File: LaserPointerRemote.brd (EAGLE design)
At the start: 24.5 x 45.5 mm, 34 parts, among them IC1 MEGA8-AI, IC2 MCP1640, J1 AVR_SPI_PRG_6NS, U1 2N7002, X1 22-05-7028-02, X3 22-23-2031

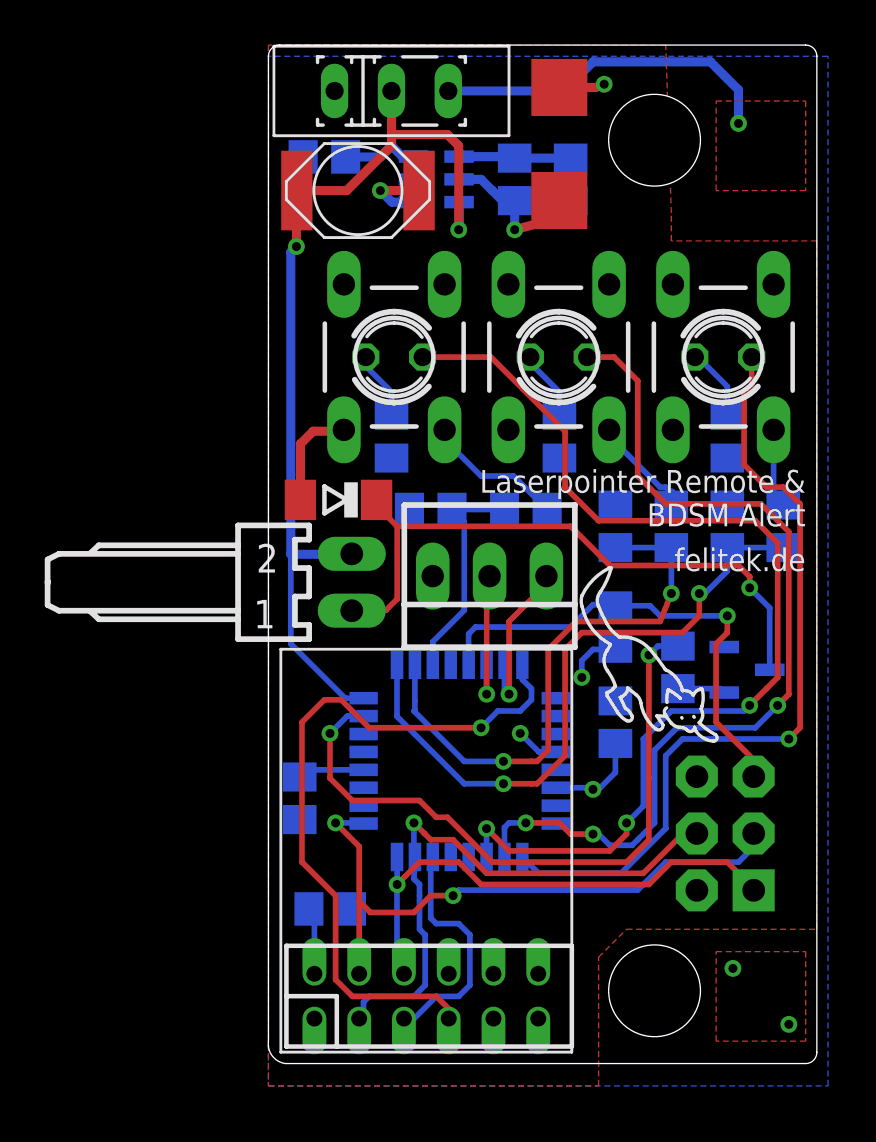
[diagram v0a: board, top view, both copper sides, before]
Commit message: Refactored PCB to fit the strapupox
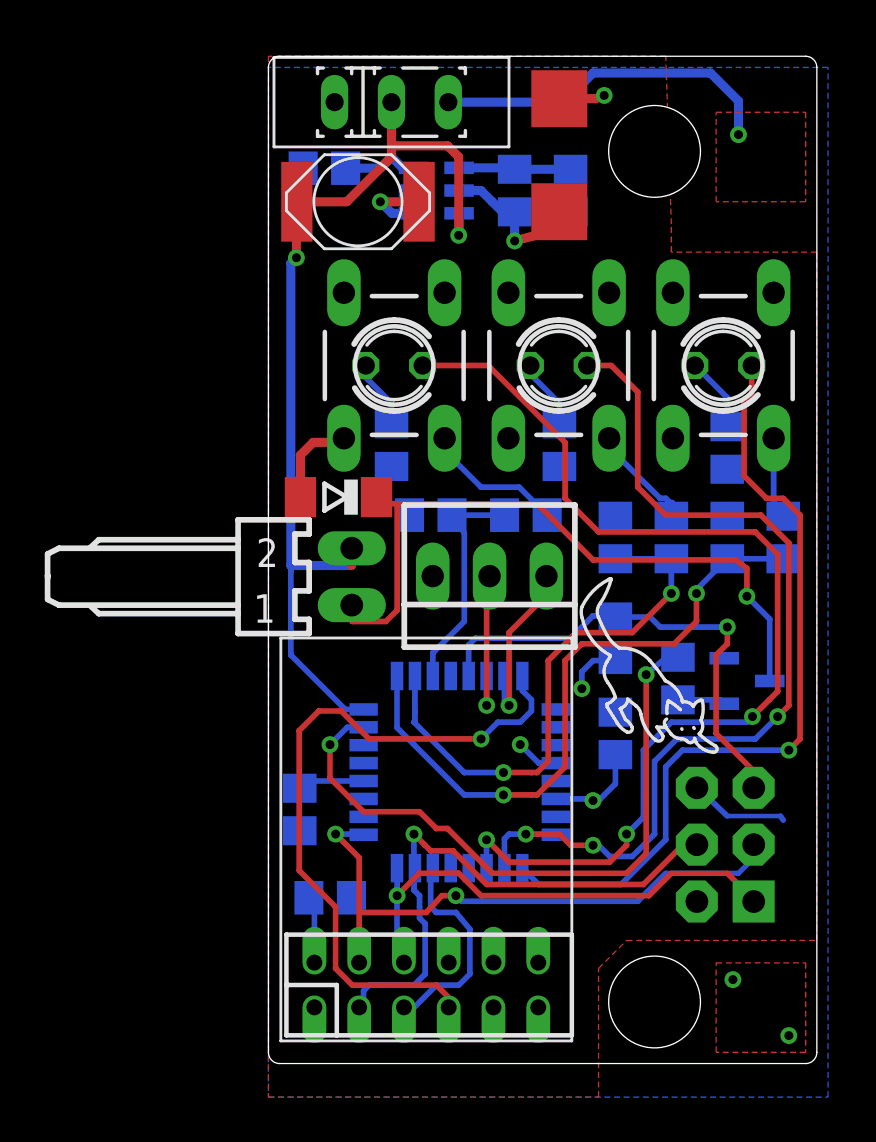
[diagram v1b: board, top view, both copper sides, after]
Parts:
- moved C1 0.50 mm to (15.5, 14.8)
- moved C2 0.50 mm to (1.40, 11.3)
- moved C3 0.50 mm to (2.76, 7.41)
- moved C4 0.50 mm to (2.50, 40.0)
- moved C5 0.50 mm to (13.0, 40.6)
- moved C6 0.50 mm to (20.5, 23.5)
- moved C7 0.50 mm to (15.5, 23.5)
- moved IC1 0.50 mm to (8.54, 13.0)
- moved IC2 0.50 mm to (7.50, 39.0)
- moved J1 0.50 mm to (20.4, 9.78)
- moved L2 0.50 mm to (4.00, 38.5)
- moved R1 0.50 mm to (15.5, 19.0)
- moved R10 0.50 mm to (18.0, 23.5)
- moved R12 0.50 mm to (23.0, 23.5)
- moved R2 0.50 mm to (18.3, 17.2)
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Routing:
- net GND: track 6.73 -> 10.7 mm
- net N$2: track 28.3 -> 31.1 mm
- net SCK: track 28.1 -> 26.9 mm
- net SEL: track 10.6 -> 9.54 mm
- net MOSI: track 25.7 -> 24.7 mm
- net MISO: track 23.7 -> 22.7 mm
- net VIN: track 49.0 -> 50.0 mm
- net INT0: track 31.6 -> 30.8 mm
- net INPUT2: track 25.1 -> 24.5 mm
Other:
- board size 24.5 x 45.5 mm -> 24.5 x 45 mm
- board text removed: "BDSM Alert"
- board text removed: "Laserpointer Remote &"

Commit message: Changed VCC to 5V instead of 3.3V Added NPN transistor instead of mosfet Connected AVCC
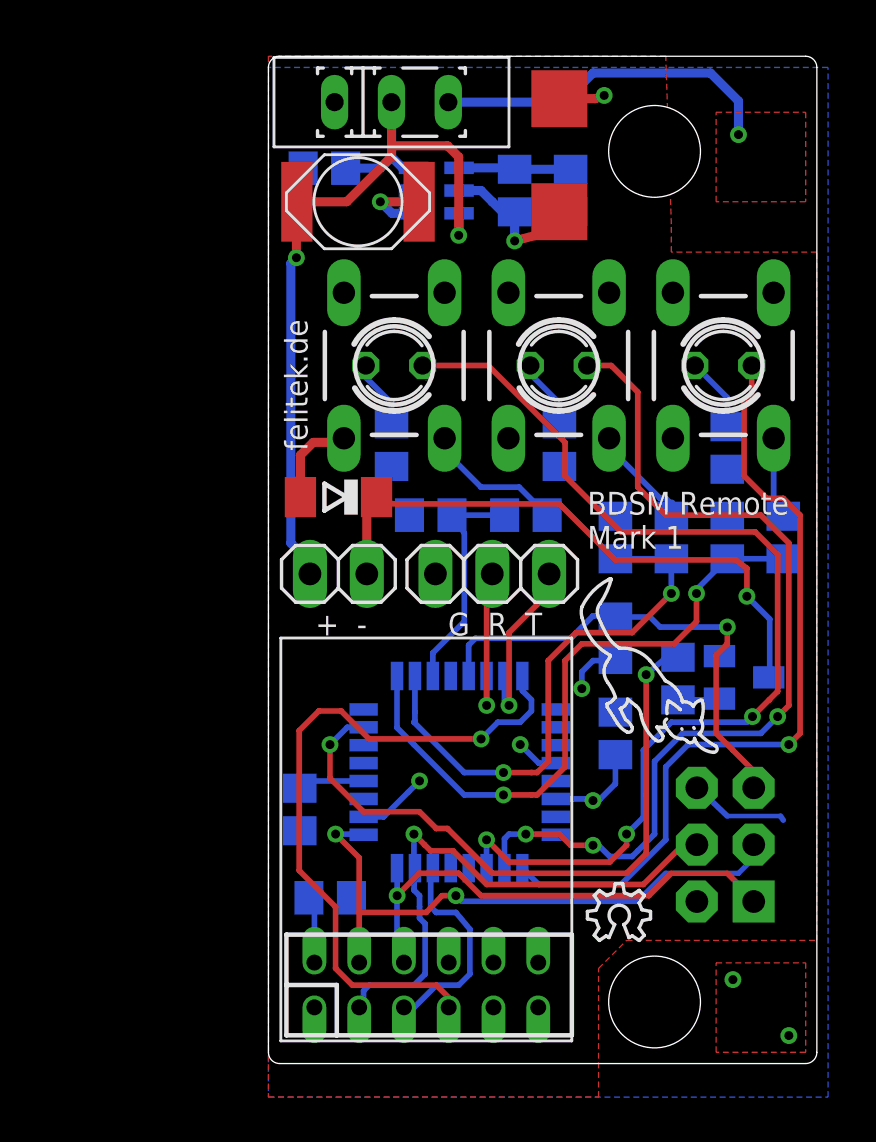
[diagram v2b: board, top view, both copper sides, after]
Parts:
- removed U1: 2N7002, SteveMarple:SOT23-3-ROTATED
- removed X1: 22-05-7028-02, con-molex:7395-02
- removed X3: 22-23-2031, con-molex:22-23-2031
- added JP1: (no value), pinhead:1X02
- added JP2: (no value), pinhead:1X03
- added T1: BC818, transistor:SOT23-BEC
- added U$2: (no value), ohw-logo:OSHW_6X100_NOTEXT
- R6: value 97.6k -> 100k
- R7: value 56.2k -> 33k
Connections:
- removed net AVCC: IC1.18
- net GND: now also JP2.3, T1.E; no longer U1.2, X3.3
- net N$1: now also T1.B; no longer U1.1
- net N$2: now also JP1.1, T1.C; no longer U1.3, X1.1
- net RXD: now also JP2.2; no longer X3.2
- net TXD: now also JP2.1; no longer X3.1
- net VCC: now also IC1.18
- net VIN: now also JP1.2; no longer IC1.24, X1.2
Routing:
- net VIN: track 50.0 -> 38.2 mm
- net N$2: track 31.1 -> 27.3 mm
- net VCC: track 18.4 -> 21.6 mm, vias 4 -> 5
- net LED3: track 46.9 -> 46.3 mm
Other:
- board text added: "+ -"
- board text added: "BDSM Remote Mark 1"
- board text added: "G R T"

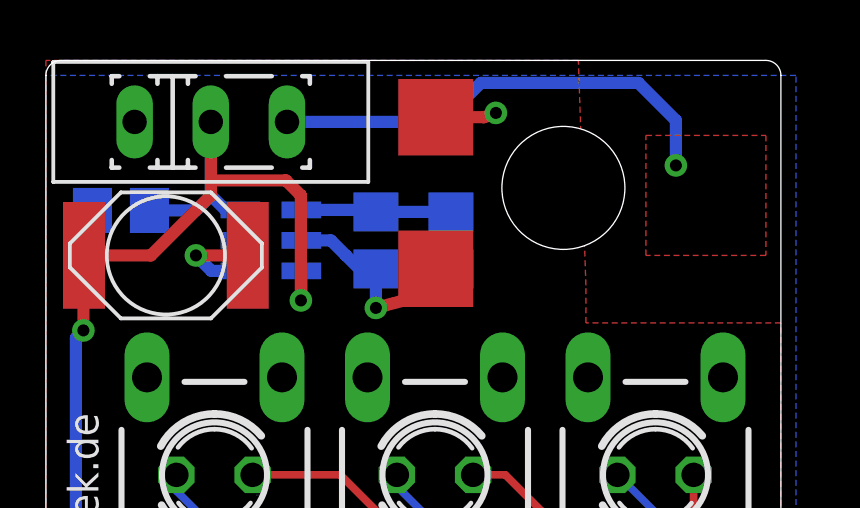
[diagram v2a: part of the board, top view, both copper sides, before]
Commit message: Use X7R output cap instead of a tantalum one
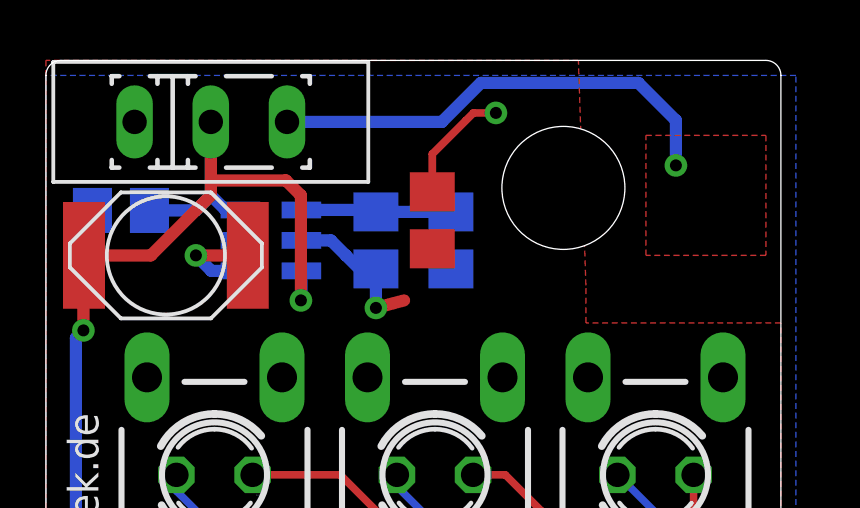
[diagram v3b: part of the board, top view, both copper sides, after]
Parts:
- C5: device rcl:C/6032-28R -> rcl:C0805
- moved C5 0.92 mm to (12.9, 39.7), turned to 90 degrees
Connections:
- net GND: now also C5.2; no longer C5.-
- net VCC: now also C5.1; no longer C5.+
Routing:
- net GND: track 10.7 -> 12.6 mm
- net VCC: track 21.6 -> 20.1 mm
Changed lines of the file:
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@@
 <grid distance="1" unitdist="mm" unit="mm" style="lines" multiple="1" display="no" altdistance="0.125" altunitdist="mm" altunit="mm"/>
 <layers>
-<layer number="1" name="Top" color="4" fill="1" visible="no" active="yes"/>
+<layer number="1" name="Top" color="4" fill="1" visible="yes" active="yes"/>
 <layer number="2" name="Route2" color="1" fill="3" visible="no" active="no"/>
 <layer number="3" name="Route3" color="4" fill="3" visible="no" active="no"/>
@@
 <layer number="14" name="Route14" color="1" fill="6" visible="no" active="no"/>
 <layer number="15" name="Route15" color="4" fill="6" visible="no" active="no"/>
-<layer number="16" name="Bottom" color="1" fill="1" visible="yes" active="yes"/>
+<layer number="16" name="Bottom" color="1" fill="1" visible="no" active="yes"/>
 <layer number="17" name="Pads" color="2" fill="1" visible="yes" active="yes"/>
 <layer number="18" name="Vias" color="2" fill="1" visible="yes" active="yes"/>
 <layer number="19" name="Unrouted" color="6" fill="1" visible="yes" active="yes"/>
 <layer number="20" name="Dimension" color="15" fill="1" visible="yes" active="yes"/>
-<layer number="21" name="tPlace" color="7" fill="1" visible="no" active="yes"/>
-<layer number="22" name="bPlace" color="7" fill="1" visible="yes" active="yes"/>
-<layer number="23" name="tOrigins" color="15" fill="1" visible="no" active="yes"/>
-<layer number="24" name="bOrigins" color="15" fill="1" visible="yes" active="yes"/>
-<layer number="25" name="tNames" color="7" fill="1" visible="no" active="yes"/>
-<layer number="26" name="bNames" color="7" fill="1" visible="yes" active="yes"/>
-<layer number="27" name="tValues" color="7" fill="1" visible="no" active="yes"/>
-<layer number="28" name="bValues" color="7" fill="1" visible="yes" active="yes"/>
+<layer number="21" name="tPlace" color="7" fill="1" visible="yes" active="yes"/>
+<layer number="22" name="bPlace" color="7" fill="1" visible="no" active="yes"/>
+<layer number="23" name="tOrigins" color="15" fill="1" visible="yes" active="yes"/>
+<layer number="24" name="bOrigins" color="15" fill="1" visible="no" active="yes"/>
+<layer number="25" name="tNames" color="7" fill="1" visible="yes" active="yes"/>
+<layer number="26" name="bNames" color="7" fill="1" visible="no" active="yes"/>
+<layer number="27" name="tValues" color="7" fill="1" visible="yes" active="yes"/>
+<layer number="28" name="bValues" color="7" fill="1" visible="no" active="yes"/>
 <layer number="29" name="tStop" color="7" fill="3" visible="no" active="yes"/>
 <layer number="30" name="bStop" color="7" fill="6" visible="no" active="yes"/>
@@
 <layer number="49" name="Reference" color="7" fill="1" visible="yes" active="yes"/>
 <layer number="50" name="dxf" color="7" fill="1" visible="no" active="no"/>
-<layer number="51" name="tDocu" color="7" fill="1" visible="no" active="yes"/>
-<layer number="52" name="bDocu" color="7" fill="1" visible="yes" active="yes"/>
+<layer number="51" name="tDocu" color="7" fill="1" visible="yes" active="yes"/>
+<layer number="52" name="bDocu" color="7" fill="1" visible="no" active="yes"/>
 <layer number="53" name="tGND_GNDA" color="7" fill="9" visible="no" active="no"/>
 <layer number="54" name="bGND_GNDA" color="1" fill="9" visible="no" active="no"/>
@@
 <attribute name="OC_TME" value="CRCW080556K2FKTABC" x="13.5" y="39" size="1.778" layer="28" rot="MR270" display="off"/>
 </element>
-<element name="C5" library="rcl" package="C/6032-28R" value="10µ" x="12.995" y="40.58" smashed="yes" rot="R270"/>
+<element name="C5" library="rcl" package="C0805" value="10µ" x="12.88" y="39.67" smashed="yes" rot="R90"/>
 <element name="S2" library="switch-tact" package="DTS-6" value="DTS-6" x="5.62" y="31.185" smashed="yes" rot="R90"/>
 <element name="S3" library="switch-tact" package="DTS-6" value="DTS-6" x="12.97" y="31.185" smashed="yes" rot="R90"/>
@@
 <contactref element="IC2" pad="2"/>
 <contactref element="R7" pad="2"/>
-<contactref element="C5" pad="-"/>
+<contactref element="C5" pad="2"/>
 <contactref element="D1" pad="A"/>
 <contactref element="R8" pad="1"/>
@@
 </polygon>
 <via x="15" y="43.25" extent="1-16" drill="0.4"/>
-<wire x1="12.995" y1="43.105" x2="14.605" y2="43.105" width="0.4064" layer="1"/>
-<wire x1="14.605" y1="43.105" x2="15" y2="43.25" width="0.4064" layer="1"/>
 <wire x1="1.43" y1="25.305" x2="1.43" y2="25.82" width="0.4064" layer="1"/>
 <wire x1="1.43" y1="25.82" x2="1.43" y2="27.18" width="0.4064" layer="1"/>
@@
 <contactref element="JP2" pad="3"/>
 <contactref element="T1" pad="E"/>
+<wire x1="12.88" y1="40.62" x2="12.88" y2="41.88" width="0.254" layer="1"/>
+<wire x1="12.88" y1="41.88" x2="14" y2="43" width="0.254" layer="1"/>
+<wire x1="15" y1="43.25" x2="14.25" y2="43.25" width="0.254" layer="1"/>
+<wire x1="14.25" y1="43.25" x2="14" y2="43" width="0.254" layer="1"/>
 </signal>
 <signal name="VCC">
@@
 <contactref element="IC2" pad="5"/>
 <contactref element="R6" pad="2"/>
-<contactref element="C5" pad="+"/>
+<contactref element="C5" pad="1"/>
 <wire x1="8.516" y1="39" x2="9.5" y2="39" width="0.4064" layer="16"/>
 <wire x1="9.5" y1="39" x2="10" y2="38.5" width="0.4064" layer="16"/>
@@
 <via x="11" y="36.75" extent="1-16" drill="0.4"/>
 <wire x1="11" y1="36.75" x2="11.94" y2="37" width="0.4064" layer="1"/>
-<wire x1="11.94" y1="37" x2="12.995" y2="38.055" width="0.4064" layer="1"/>
 <wire x1="2.0537" y1="4.5099" x2="2.0537" y2="7.1601" width="0.254" layer="16"/>
 <wire x1="2.0537" y1="7.1601" x2="1.8087" y2="7.4051" width="0.254" layer="16"/>
